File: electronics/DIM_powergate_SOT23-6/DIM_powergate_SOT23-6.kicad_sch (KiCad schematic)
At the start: 10 parts, among them J1 Conn_01x04, J2 Conn_01x04, Q1 PMOS, Q2 NMOS

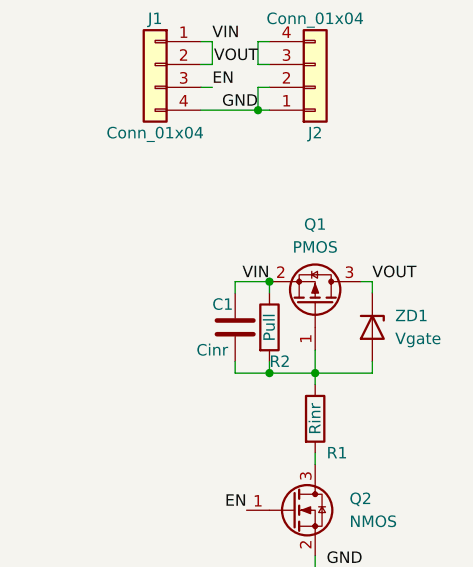
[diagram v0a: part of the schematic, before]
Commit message: updated SOT23 power gate, added SOT23-6 power gate module
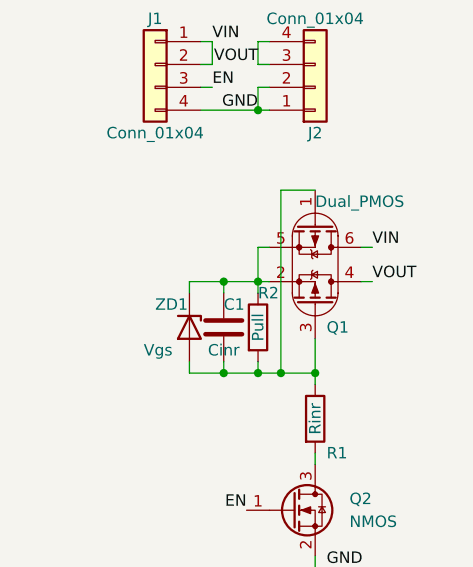
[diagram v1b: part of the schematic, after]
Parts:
- removed Q1: PMOS, SquantorIC:SOT23-3, symbol Transistor_FET:Q_PMOS_GSD
- added Q1: Dual_PMOS, SquantorIC:SOT23-6-HAND, symbol SquantorDevice:Q_PMOS_dual_6pin_SOT23
- ZD1: value Vgate -> Vgs
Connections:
- net VIN: now also Q1.6 (D1); no longer C1.1, R2.1
- net VOUT: now also Q1.4 (D2); no longer ZD1.1 (K)
- net at C1.2, R1.1, R2.2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: now also Q1.1 (G1), Q1.3 (G2)
- new net: C1.1, Q1.2 (S2), Q1.5 (S1), R2.1, ZD1.1 (K)
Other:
- moved on the sheet: C1, R2, ZD1

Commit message: Reviewed and fixed
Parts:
- N1: value 20260103 -> 20260110
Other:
- note added: "Connections"
- note added: "Switch"
- moved on the sheet: C1, J1, J2, Q1, Q2, R1, R2, ZD1

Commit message: preparation for production V20260118
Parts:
- N1: value 20260110 -> 20260118
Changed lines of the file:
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@@
 			)
 		)
-		(property "Value" "20260110"
+		(property "Value" "20260118"
 			(at 20.32 189.23 0)
 			(effects
